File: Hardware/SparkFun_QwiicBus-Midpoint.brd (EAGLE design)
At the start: 45.7 x 27.9 mm, 73 parts, among them J1 QWIIC, J2 QWIIC, J3 RJ45, J7 RJ45, U1 PCA9615, U3 LMR33630

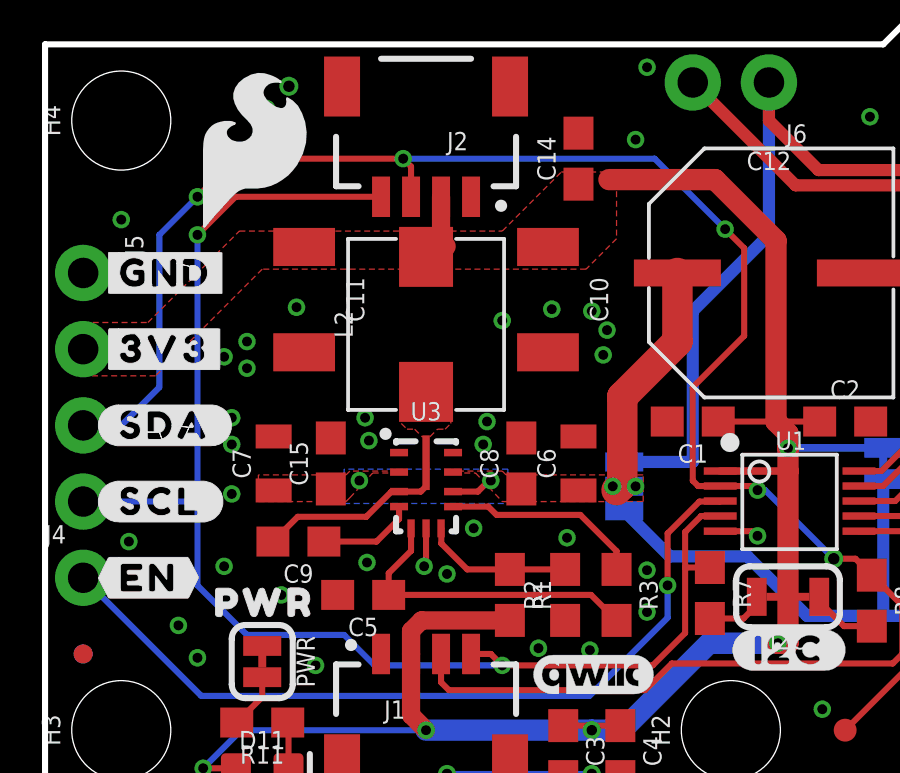
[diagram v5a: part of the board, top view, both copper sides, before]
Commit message: initial layout of hot swap controller
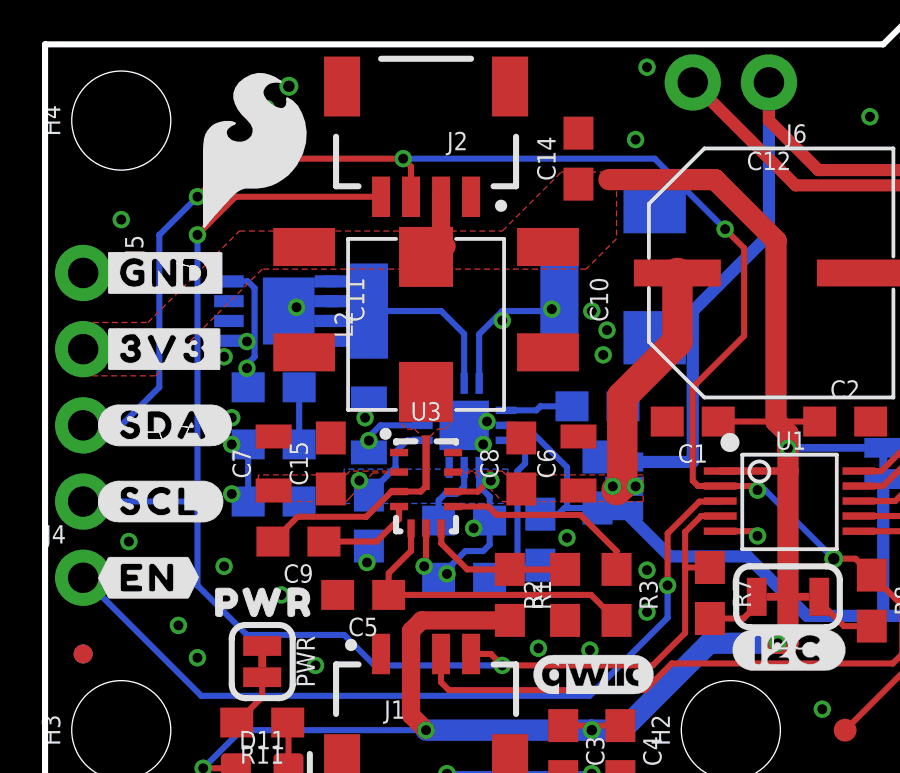
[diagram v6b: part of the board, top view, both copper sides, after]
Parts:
- added C13: 20nF, hotswap:0603
- added C17: 39nF, hotswap:0805
- added D1: SMAJ36A, hotswap:DO-214AC
- added FRAME2: FRAME-LETTER, SparkFun-Aesthetics:CREATIVE_COMMONS
- added Q1: SI7120AD, hotswap:1212-8
- added R10: 23m, hotswap:2512
- added R12: 10, SparkFun-Resistors:0603
- added R13: 1k, SparkFun-Resistors:0603
- added R14: 20k, SparkFun-Resistors:0603
- added R15: 1M, SparkFun-Resistors:0603
- added R4: 1.65K, hotswap:0603
- added R5: 32.4k, hotswap:0603
- added R6: 4.22k, hotswap:0603
- added R9: 1020K, hotswap:0603
- added U4: LTC4231 Hot Swap Controller, hotswap:QFN-12
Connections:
- new net N$10: R4.2, R9.1, U4.2
- new net N$11: Q1.4, R12.2
- new net N$12: Q1.5, Q1.6, Q1.7, Q1.8, Q1.PAD, R10.P$2, U4.11
- new net N$16: R12.1, R13.2, U4.10
- new net N$17: C13.1, R13.1
- new net N$19: R14.1, U4.7
- new net N$2: R5.1, U4.5
- new net N$20: R15.1, U4.1
- new net N$21: C17.1, U4.8
- new net N$5: R5.2, R6.1, U4.4
- new net N$8: R4.1, R6.2, U4.3
- new net PWR_SRC: D1.C, PSEL.2, R10.P$1, R15.2, R9.2, U4.12
- net GND: now also C13.2, C17.2, D1.A, U4.6, U4.EXP
- net VREG_IN: now also Q1.1, Q1.2, Q1.3, R14.2, U4.9; no longer PSEL.2
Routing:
- net N$12: track 0.00 -> 11.1 mm
- net N$8: track 0.00 -> 6.70 mm
- net N$10: track 0.00 -> 5.96 mm
- net N$5: track 0.00 -> 4.88 mm
- net PWR_SRC: track 0.00 -> 4.63 mm
- net N$11: track 0.00 -> 4.34 mm
- net N$19: track 0.00 -> 2.85 mm
- net N$2: track 0.00 -> 2.64 mm
- net N$21: track 0.00 -> 2.45 mm
- net N$20: track 0.00 -> 2.25 mm
- net N$17: track 0.00 -> 1.91 mm
- net N$16: track 0.00 -> 1.90 mm

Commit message: finish routing
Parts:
- moved PSEL 1.02 mm to (20.3, 11.9)
- moved C13 1.02 mm to (7.62, 10.4)
- moved C7 0.76 mm to (6.86, 12.7)
- moved R6 0.63 mm to (14.0, 8.26)
- moved C9 0.38 mm to (8.45, 9.72)
- moved C8 0.25 mm to (16.1, 12.7)
- moved C5 0.25 mm to (10.6, 8.06)
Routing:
- net 3.3V: track 61.9 -> 37.8 mm
- net VREG_IN: track 9.82 -> 28.7 mm, vias 4 -> 3
- net PWR_SRC: track 4.63 -> 15.6 mm
- net N$16: track 1.90 -> 7.71 mm
- net VCC_1: track 59.9 -> 58.9 mm
- net N$17: track 1.91 -> 2.92 mm
- net SDA: track 67.0 -> 67.8 mm
- net VCC_2: track 55.5 -> 54.7 mm
- net EN: track 27.2 -> 27.7 mm
- net GND: vias 44 -> 45
- added copper zone on layer 15, net 3.3V
- added copper zone on layer 2, net GND
- added copper zone on layer 2, net VREG_IN
- removed copper zone on layer 1, net 3.3V
- removed copper zone on layer 16, net VREG_IN

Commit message: pushing unsaved silk changes
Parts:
- moved U$15 16.5 mm to (28.2, 13.5), turned to 270 degrees
- moved U$30 7.12 mm to (24.0, 8.51), turned to 90 degrees
- moved U$17 1.02 mm to (22.0, 14.5)
- moved U$18 0.76 mm to (20.1, 10.9)
- moved U$19 0.64 mm to (20.0, 15.2)
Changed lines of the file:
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@@
 <?xml version="1.0" encoding="utf-8"?>
 <!DOCTYPE eagle SYSTEM "eagle.dtd">
-<eagle version="9.3.1">
+<eagle version="9.6.0">
 <drawing>
 <settings>
@@
 <grid distance="0.05" unitdist="inch" unit="inch" style="lines" multiple="1" display="yes" altdistance="0.005" altunitdist="inch" altunit="inch"/>
 <layers>
-<layer number="1" name="Top" color="4" fill="1" visible="yes" active="yes"/>
-<layer number="2" name="Route2" color="1" fill="3" visible="yes" active="yes"/>
+<layer number="1" name="Top" color="4" fill="1" visible="no" active="yes"/>
+<layer number="2" name="Route2" color="1" fill="3" visible="no" active="yes"/>
 <layer number="3" name="Route3" color="4" fill="3" visible="no" active="no"/>
 <layer number="4" name="Route4" color="1" fill="4" visible="no" active="no"/>
@@
 <attribute name="VALUE" x="25.4" y="27.432" size="0.6096" layer="27" font="vector" ratio="20" rot="R180"/>
 </element>
-<element name="U$30" library="output" package="MIDPOINT0" value="" x="18.161" y="12.573" smashed="yes" rot="MR0"/>
-<element name="U$15" library="QwiicBus#working#Logo#jpg (2)" package="QWIICBUS#WORKING#LOGO#JPG" value="" x="12.192" y="17.526" smashed="yes" rot="MR0"/>
+<element name="U$30" library="output" package="MIDPOINT0" value="" x="24.003" y="8.509" smashed="yes" rot="MR90"/>
+<element name="U$15" library="QwiicBus#working#Logo#jpg (2)" package="QWIICBUS#WORKING#LOGO#JPG" value="" x="28.194" y="13.462" smashed="yes" rot="MR270"/>
 <element name="LOGO3" library="SparkFun-Aesthetics" package="SFE_LOGO_FLAME_.2" value="SFE_LOGO_FLAME.2_INCH" x="6.985" y="23.114" smashed="yes"/>
 <element name="LOGO4" library="SparkFun-Aesthetics" package="SFE_LOGO_NAME_FLAME_.1" value="SFE_LOGO_NAME_FLAME.1_INCH" x="12.7" y="21.59" smashed="yes" rot="MR0"/>
@@
 <element name="U$16" library="output" package="#VCC2#0" value="" x="24.13" y="24.8285" smashed="yes" rot="MR270"/>
 <element name="U$24" library="output" package="#GND2#0" value="" x="21.59" y="24.892" smashed="yes" rot="MR270"/>
-<element name="U$17" library="output" package="#PSEL#0" value="" x="20.955" y="14.605" smashed="yes" rot="MR270"/>
-<element name="U$18" library="output" package="10" value="" x="19.304" y="10.8585" smashed="yes" rot="MR270"/>
-<element name="U$19" library="output" package="20" value="" x="19.3675" y="15.1765" smashed="yes" rot="MR270"/>
+<element name="U$17" library="output" package="#PSEL#0" value="" x="21.971" y="14.478" smashed="yes" rot="MR270"/>
+<element name="U$18" library="output" package="10" value="" x="20.066" y="10.8585" smashed="yes" rot="MR270"/>
+<element name="U$19" library="output" package="20" value="" x="20.0025" y="15.1765" smashed="yes" rot="MR270"/>
 <element name="TP1" library="SparkFun-Connectors" package="PAD.03X.03" value="TEST-POINT3" x="26.67" y="3.81" smashed="yes"/>
 <element name="U$11" library="output" package="#GND2#0" value="" x="36.83" y="22.2885" smashed="yes" rot="MR90"/>
